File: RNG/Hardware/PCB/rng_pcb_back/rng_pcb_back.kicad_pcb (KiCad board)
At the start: 2 copper layers, 50 x 100 mm, 28 parts, among them J10 Conn_01x08_Socket, J11 Eurorack_2x8_Power, J7 Conn_01x07_Socket, J8 Conn_02x03_Socket, J9 Conn_01x06_Socket, U1 TLC5940NT, U2 MCP4922, U3 MCP6004, U4 TL072, U5 LM4040BCZ-5

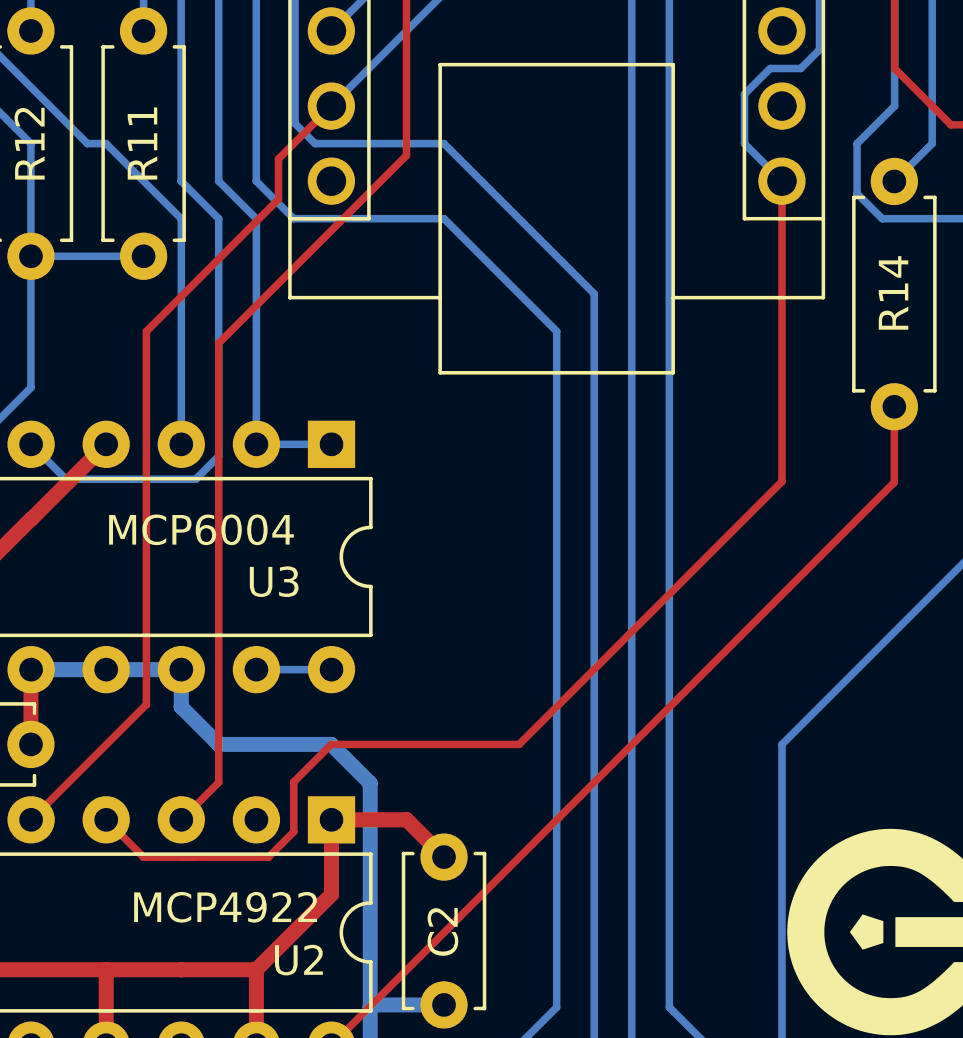
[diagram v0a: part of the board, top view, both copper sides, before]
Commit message: Fix some issues with RNG and DD PCBs (closes #6)
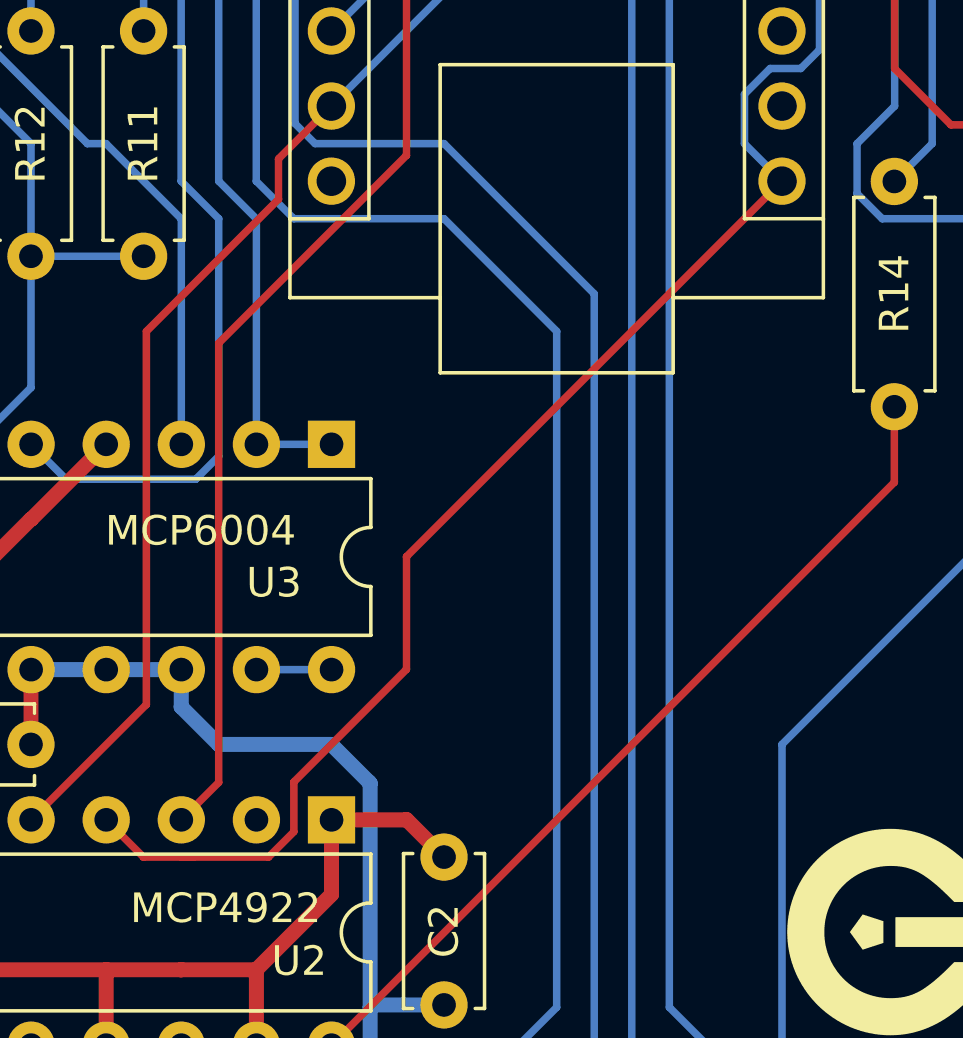
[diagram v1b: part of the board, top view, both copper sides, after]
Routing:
- net SPI_SCK: track 100.9 -> 97.2 mm
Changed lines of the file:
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@@
   (segment (start 43.18 111.76) (end 49.53 105.41) (width 0.254) (layer "B.Cu") (net 14))
   (segment (start 35.565 135.9) (end 36.825 137.16) (width 0.254) (layer "F.Cu") (net 16))
+  (segment (start 41.055187 137.16) (end 41.91 136.305187) (width 0.254) (layer "F.Cu") (net 16))
   (segment (start 38.1 137.16) (end 38.515187 137.16) (width 0.254) (layer "F.Cu") (net 16))
-  (segment (start 41.91 134.62) (end 41.91 136.305187) (width 0.254) (layer "F.Cu") (net 16))
+  (segment (start 45.72 130.81) (end 45.72 127) (width 0.254) (layer "F.Cu") (net 16))
   (segment (start 36.825 137.16) (end 36.83 137.16) (width 0.254) (layer "F.Cu") (net 16))
-  (segment (start 43.18 133.35) (end 41.91 134.62) (width 0.254) (layer "F.Cu") (net 16))
   (segment (start 36.83 137.16) (end 38.1 137.16) (width 0.254) (layer "F.Cu") (net 16))
-  (segment (start 41.91 136.305187) (end 41.055187 137.16) (width 0.254) (layer "F.Cu") (net 16))
-  (segment (start 58.42 124.46) (end 49.53 133.35) (width 0.254) (layer "F.Cu") (net 16))
-  (segment (start 41.055187 137.16) (end 38.1 137.16) (width 0.254) (layer "F.Cu") (net 16))
-  (segment (start 58.42 114.3) (end 58.42 124.46) (width 0.254) (layer "F.Cu") (net 16))
-  (segment (start 49.53 133.35) (end 43.18 133.35) (width 0.254) (layer "F.Cu") (net 16))
+  (segment (start 41.91 136.305187) (end 41.91 134.62) (width 0.254) (layer "F.Cu") (net 16))
+  (segment (start 38.1 137.16) (end 41.055187 137.16) (width 0.254) (layer "F.Cu") (net 16))
+  (segment (start 45.72 127) (end 58.42 114.3) (width 0.254) (layer "F.Cu") (net 16))
+  (segment (start 41.91 134.62) (end 45.72 130.81) (width 0.254) (layer "F.Cu") (net 16))
   (segment (start 57.15 70.729813) (end 57.15 72.39) (width 0.254) (layer "B.Cu") (net 16))
   (segment (start 57.15 72.39) (end 50.8 78.74) (width 0.254) (layer "B.Cu") (net 16))
